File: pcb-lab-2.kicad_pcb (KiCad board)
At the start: 2 copper layers, 35.3 x 23.6 mm, 27 parts, among them J1 Conn_01x02, J2 Conn_01x02, J3 Conn_01x02, J4 Conn_01x02, J5 Conn_01x02, J6 Conn_01x02, J7 Conn_01x02, J8 Conn_01x02, J9 USB_B_Micro, Q1 FDV302P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

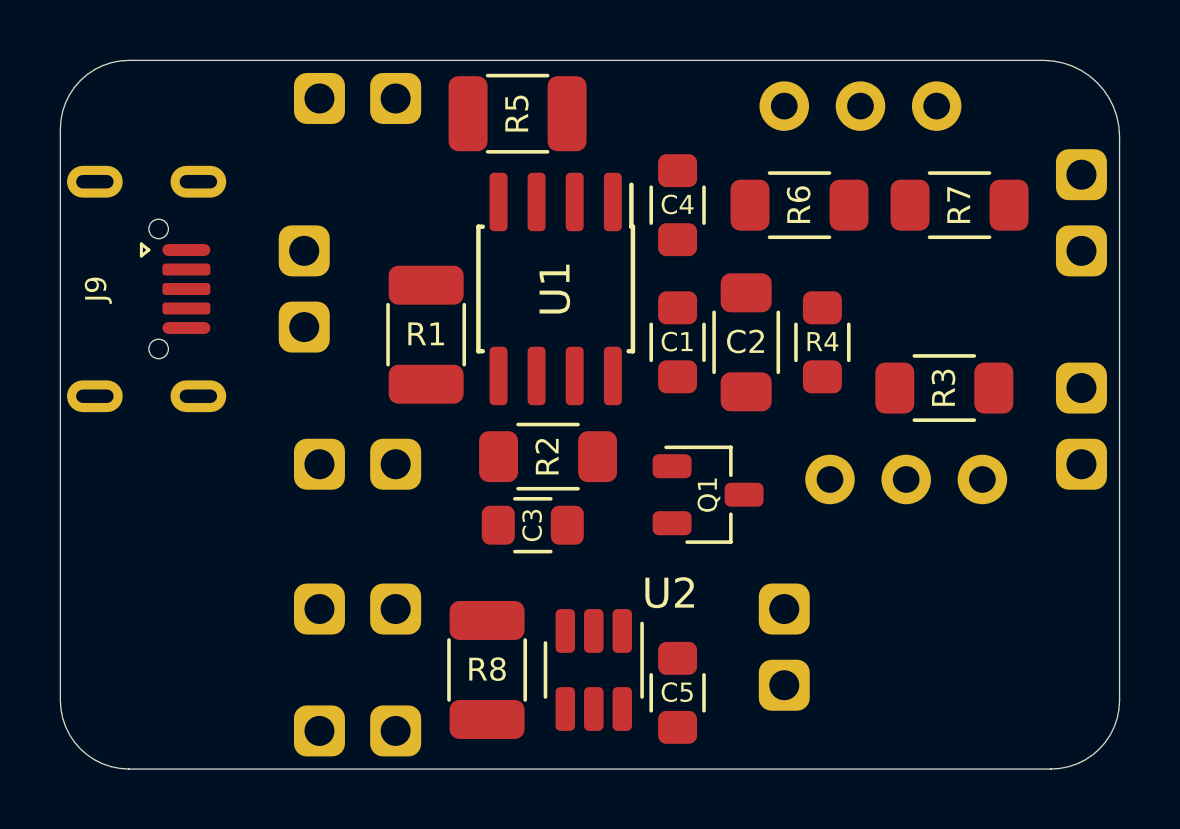
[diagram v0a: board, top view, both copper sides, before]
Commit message: Make board smaller
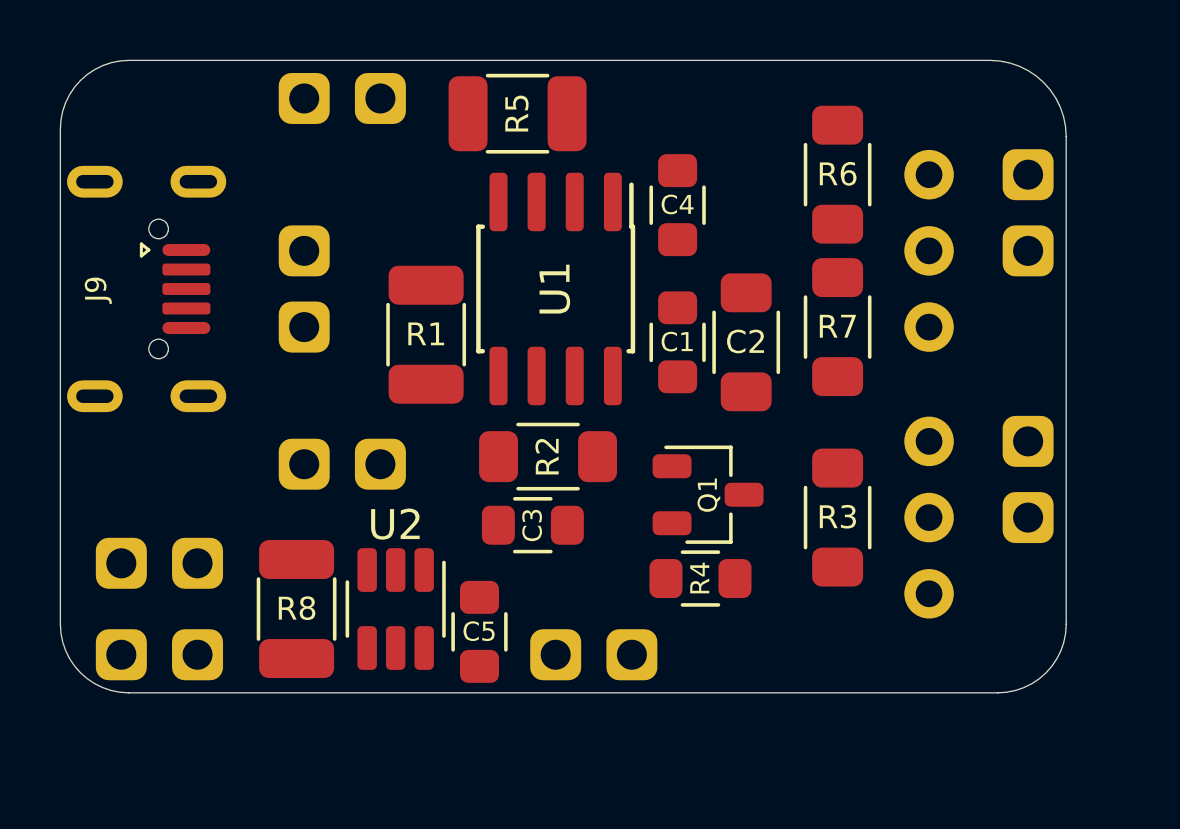
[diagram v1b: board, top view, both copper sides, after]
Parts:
- moved R4 8.86 mm to (152.1, 137.7), turned to 0 degrees
- moved J8 7.77 mm to (147.3, 140.2), turned to 270 degrees
- moved J7 7.08 mm to (132.8, 140.2)
- moved U2 6.91 mm to (142.0, 138.7)
- moved C5 6.91 mm to (144.8, 139.4), turned to 270 degrees
- moved J6 6.78 mm to (132.8, 137.2)
- moved R8 6.67 mm to (138.7, 138.7)
- moved R7 5.75 mm to (156.7, 129.3), turned to 270 degrees
- moved R3 5.59 mm to (156.7, 135.6), turned to 270 degrees
- moved RV2 5.34 mm to (159.8, 126.7), turned to 0 degrees
- moved J3 2.51 mm to (163.1, 133.1)
- moved J5 1.78 mm to (163.1, 124.2)
- moved R6 1.63 mm to (156.7, 124.2), turned to 270 degrees
- moved RV1 1.48 mm to (159.8, 135.6), turned to 0 degrees
- moved J2 0.51 mm to (138.9, 133.9)
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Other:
- board size 35.3 x 23.6 mm -> 33.5 x 21.1 mm

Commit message: Complete routing
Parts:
- moved R5 2.59 mm to (143.7, 123.3), turned to 60 degrees
- moved C3 0.25 mm to (146.6, 136.1)
- moved R4 0.25 mm to (152.4, 137.7), turned to 180 degrees
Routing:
- net V+: track 0.00 -> 56.0 mm, vias 0 -> 2
- net GND: track 0.00 -> 39.6 mm, vias 0 -> 10
- net Net-(C4-Pad2): track 0.00 -> 15.5 mm
- net VOUT1: track 0.00 -> 15.3 mm
- net Net-(C3-Pad1): track 0.00 -> 14.8 mm
- net Net-(C3-Pad2): track 0.00 -> 12.3 mm
- net V3+: track 0.00 -> 11.2 mm
- net V3-: track 0.00 -> 11.2 mm
- net VOUT2: track 0.00 -> 10.2 mm
- net V2-: track 0.00 -> 8.51 mm
- net V1-: track 0.00 -> 7.28 mm
- net VOUT3: track 0.00 -> 7.11 mm, vias 0 -> 1
- added copper zone on B.Cu, net GND

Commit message: Add silkscreen
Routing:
- net GND: track 39.6 -> 43.6 mm, vias 10 -> 13
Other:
- board text added: "(C) Vlad Belous CC BY-SA 4.0"
- board text added: "G"
- board text added: "GND"
- board text added: "High-side"
- board text added: "Low-side"
- board text added: "Low-side gain: High-side gain: INA181 gain:"
- board text added: "PCB Lab #2: current sensing"
- board text added: "V+"
- board text added: "V-"
- board text added: "V2-"
- board text added: "V3+ G"
- board text added: "V3- G"
- board text added: "VOUT1"
- board text added: "VOUT2"
- board text added: "VOUT3"
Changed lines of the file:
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@@
   (general
     (thickness 1.6)
-    (drawings 10)
-    (tracks 183)
+    (drawings 31)
+    (tracks 191)
     (zones 0)
     (modules 27)
@@
   )
   (setup
-    (last_trace_width 0.3048)
+    (last_trace_width 0.508)
     (user_trace_width 0.2032)
     (user_trace_width 0.3048)
@@
     (tags "resistor 1206")
     (attr smd)
-    (fp_text reference C2 (at 0 0) (layer F.SilkS)
+    (fp_text reference C2 (at -0.2032 0) (layer F.SilkS)
       (effects (font (size 0.762 0.762) (thickness 0.1016)))
     )
@@
     (tags "resistor 0805")
     (attr smd)
-    (fp_text reference C3 (at 0 0 90) (layer F.SilkS)
+    (fp_text reference C3 (at 0 0 270) (layer F.SilkS)
       (effects (font (size 0.635 0.635) (thickness 0.1016)))
     )
@@
     (tags "usb micro receptacle")
     (attr smd)
-    (fp_text reference J9 (at 0 -1.2 90) (layer F.SilkS)
+    (fp_text reference J9 (at 0 -1.2 180) (layer F.SilkS)
       (effects (font (size 0.7 0.7) (thickness 0.15)))
     )
@@
     (tags "resistor 1206")
     (attr smd)
-    (fp_text reference R2 (at 0 0 90) (layer F.SilkS)
+    (fp_text reference R2 (at 0 0 180) (layer F.SilkS)
       (effects (font (size 0.762 0.762) (thickness 0.1016)))
     )
@@
     (tags "SOIC 1.27")
     (attr smd)
-    (fp_text reference U1 (at 0 0 270) (layer F.SilkS)
+    (fp_text reference U1 (at 0 0) (layer F.SilkS)
       (effects (font (size 1 1) (thickness 0.15)))
     )
@@
     (tags SOT-23-6)
     (attr smd)
-    (fp_text reference U2 (at -2.794 0 180) (layer F.SilkS)
-      (effects (font (size 1 1) (thickness 0.15)))
+    (fp_text reference U2 (at -2.54 -1.778 180) (layer F.SilkS)
+      (effects (font (size 0.762 0.762) (thickness 0.127)))
     )
     (fp_text value INA181 (at 0 2.9 90) (layer F.Fab) hide
@@
       (rotate (xyz 0 0 0))
     )
+  )
+  (gr_circle (center 149.225 126.7206) (end 149.1742 126.5936) (layer F.SilkS) (width 0.0762))
+  (gr_text High-side (at 139.9794 135.5344) (layer F.SilkS)
+    (effects (font (size 0.762 0.762) (thickness 0.127)))
+  )
+  (gr_text V- (at 141.224 123.444) (layer F.SilkS)
+    (effects (font (size 0.762 0.762) (thickness 0.127)))
+  )
+  (gr_text V+ (at 138.684 123.444) (layer F.SilkS)
+    (effects (font (size 0.762 0.762) (thickness 0.127)))
+  )
+  (gr_text V+ (at 140.9446 126.746) (layer F.SilkS)
+    (effects (font (size 0.762 0.762) (thickness 0.127)))
+  )
+  (gr_text G (at 140.7414 129.3114) (layer F.SilkS)
+    (effects (font (size 0.762 0.762) (thickness 0.127)))
+  )
+  (gr_text G (at 141.224 132.08) (layer F.SilkS)
+    (effects (font (size 0.762 0.762) (thickness 0.127)))
+  )
+  (gr_text V2- (at 139.192 132.08) (layer F.SilkS)
+    (effects (font (size 0.762 0.762) (thickness 0.127)))
+  )
+  (gr_text "V3- G" (at 133.858 135.128) (layer F.SilkS)
+    (effects (font (size 0.762 0.762) (thickness 0.127)))
+  )
+  (gr_text "V3+ G" (at 133.858 133.858) (layer F.SilkS)
+    (effects (font (size 0.762 0.762) (thickness 0.127)))
+  )
+  (gr_text VOUT3 (at 147.574 138.43) (layer F.SilkS)
+    (effects (font (size 0.762 0.762) (thickness 0.127)))
+  )
+  (gr_text GND (at 152.146 140.208) (layer F.SilkS)
+    (effects (font (size 0.762 0.762) (thickness 0.127)))
+  )
+  (gr_text VOUT2 (at 162.306 131.318) (layer F.SilkS)
+    (effects (font (size 0.762 0.762) (thickness 0.127)))
+  )
+  (gr_text GND (at 162.814 137.668) (layer F.SilkS)
+    (effects (font (size 0.762 0.762) (thickness 0.127)))
+  )
+  (gr_text GND (at 162.814 128.778) (layer F.SilkS)
+    (effects (font (size 0.762 0.762) (thickness 0.127)))
+  )
+  (gr_text VOUT1 (at 162.052 122.428) (layer F.SilkS)
+    (effects (font (size 0.762 0.762) (thickness 0.127)))
+  )
+  (gr_text Low-side (at 134.874 121.666) (layer F.SilkS)
+    (effects (font (size 0.762 0.762) (thickness 0.127)))
+  )
+  (gr_poly (pts (xy 148.59 133.096) (xy 143.002 133.096) (xy 143.002 132.334) (xy 141.224 132.334) (xy 141.224 126.492) (xy 148.59 126.492)) (layer B.SilkS) (width 0.1))
+  (gr_text "Low-side gain:\n\nHigh-side gain:\n\nINA181 gain:" (at 148.8948 129.794) (layer B.SilkS)
+    (effects (font (size 0.762 0.762) (thickness 0.127)) (justify right mirror))
+  )
+  (gr_text "PCB Lab #2: current sensing" (at 149.9616 125.3236) (layer B.SilkS)
+    (effects (font (size 0.762 0.762) (thickness 0.127)) (justify mirror))
+  )
+  (gr_text "(C) Vlad Belous\nCC BY-SA 4.0" (at 154.1018 122.555) (layer B.SilkS)
+    (effects (font (size 0.762 0.762) (thickness 0.127)) (justify mirror))
   )
   (dimension 21.082 (width 0.15) (layer Dwgs.User)
@@
   (segment (start 141.986 139.984) (end 141.986 138.684006) (width 0.3048) (layer F.Cu) (net 1))
   (segment (start 141.986 137.384) (end 141.986 138.684006) (width 0.3048) (layer F.Cu) (net 1))
+  (via (at 145.3896 126.6698) (size 0.7366) (drill 0.381) (layers F.Cu B.Cu) (net 1))
+  (segment (start 145.415 125.116) (end 145.415 126.6444) (width 0.508) (layer F.Cu) (net 1))
+  (segment (start 145.415 126.6444) (end 145.3896 126.6698) (width 0.508) (layer F.Cu) (net 1))
+  (segment (start 151.384 128.644) (end 151.264 128.644) (width 0.508) (layer F.Cu) (net 1))
+  (segment (start 151.264 128.644) (end 150.4442 129.4638) (width 0.508) (layer F.Cu) (net 1))
+  (via (at 150.4442 129.4638) (size 0.7366) (drill 0.381) (layers F.Cu B.Cu) (net 1))
+  (segment (start 153.67 128.144) (end 153.67 129.286) (width 0.508) (layer F.Cu) (net 1))
+  (via (at 153.67 129.286) (size 0.7366) (drill 0.381) (layers F.Cu B.Cu) (net 1))
   (segment (start 135.01 126.716) (end 136.114 126.716) (width 0.3048) (layer F.Cu) (net 2))
   (segment (start 138.908 126.716) (end 138.938 126.746) (width 0.508) (layer F.Cu) (net 2))
